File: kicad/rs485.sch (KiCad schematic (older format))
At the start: 7 parts

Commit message: Come back to moldova to finish schematics and begin layout
I've started again from Moldova to discuss with Alexander the details.
I'm now working with schematics requeriments.
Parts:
- U: renamed from U?; value LTC2866 -> LTC2865; footprint (none) -> Package_SO:SSOP-28_5.3x10.2mm_P0.65mm; symbol servo:LTC2866 -> servo:LTC2865
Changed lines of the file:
@@
 $Descr A4 11693 8268
 encoding utf-8
-Sheet 13 16
+Sheet 13 17
 Title "RS485"
 Date "25 10 2019"
@@
 $EndDescr
 $Comp
-L servo:LTC2866 U?
+L servo:LTC2865 U?
 U 1 1 5E1BEB46
 P 3500 2250
 AR Path="/5DE3DF56/5E1BEB46" Ref="U?"  Part="1"
-AR Path="/5E1BAEAA/5E1BEB46" Ref="U?"  Part="1"
-F 0 "U?" H 3500 3050 50  0000 C CNN
-F 1 "LTC2866" H 3500 2950 50  0000 C CNN
-F 2 "" H 4500 1550 50  0001 C CIN
+AR Path="/5E1BAEAA/5E1BEB46" Ref="U"  Part="1"
+F 0 "U" H 3500 3050 50  0000 C CNN
+F 1 "LTC2865" H 3500 2950 50  0000 C CNN
+F 2 "Package_SO:SSOP-28_5.3x10.2mm_P0.65mm" H 4500 1550 50  0001 C CIN
 F 3 "../doc/datasheets/ltc2865.pdf" H 3500 2250 50  0001 C CNN
 	1    3500 2250

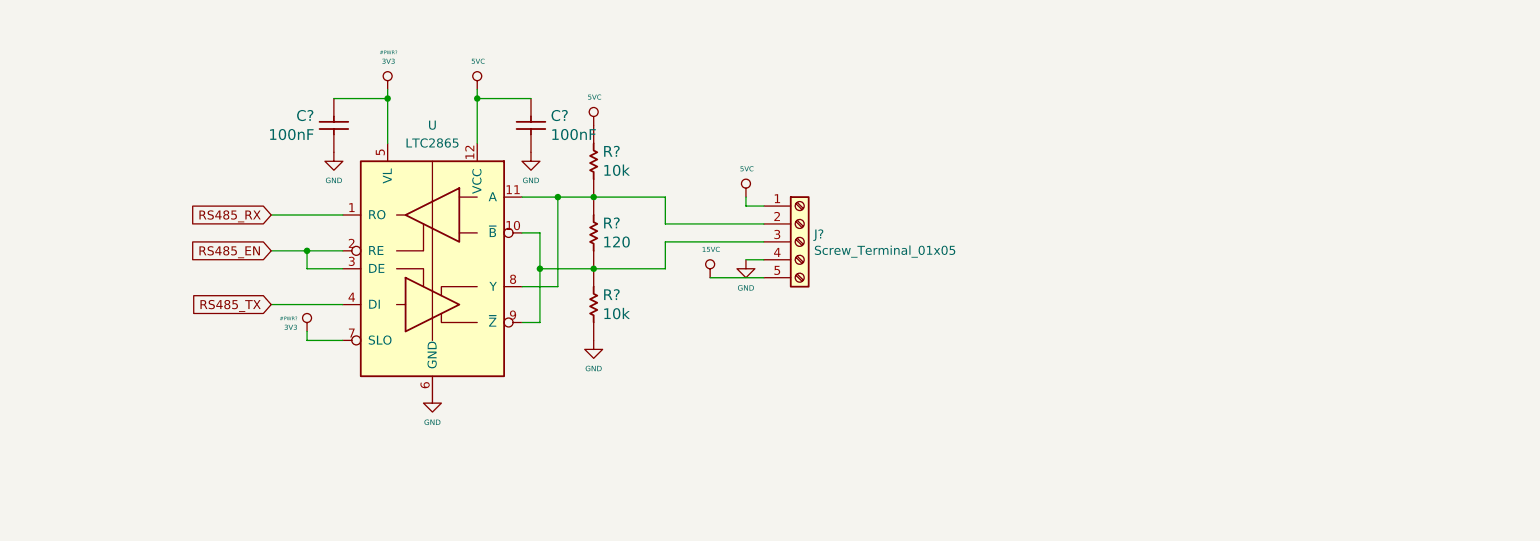
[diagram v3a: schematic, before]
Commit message: changes on ac-in ac/dc -> dc/dc
I've decided to drop out the ac/dc off-line power supply  and include it
on power board. So the MCU board only receive TWO isolated dc voltages in the rango of
8 to 20v and then it generates 5/3v3/1.2 cold and 5v/3v3 hot to the
circuitery.
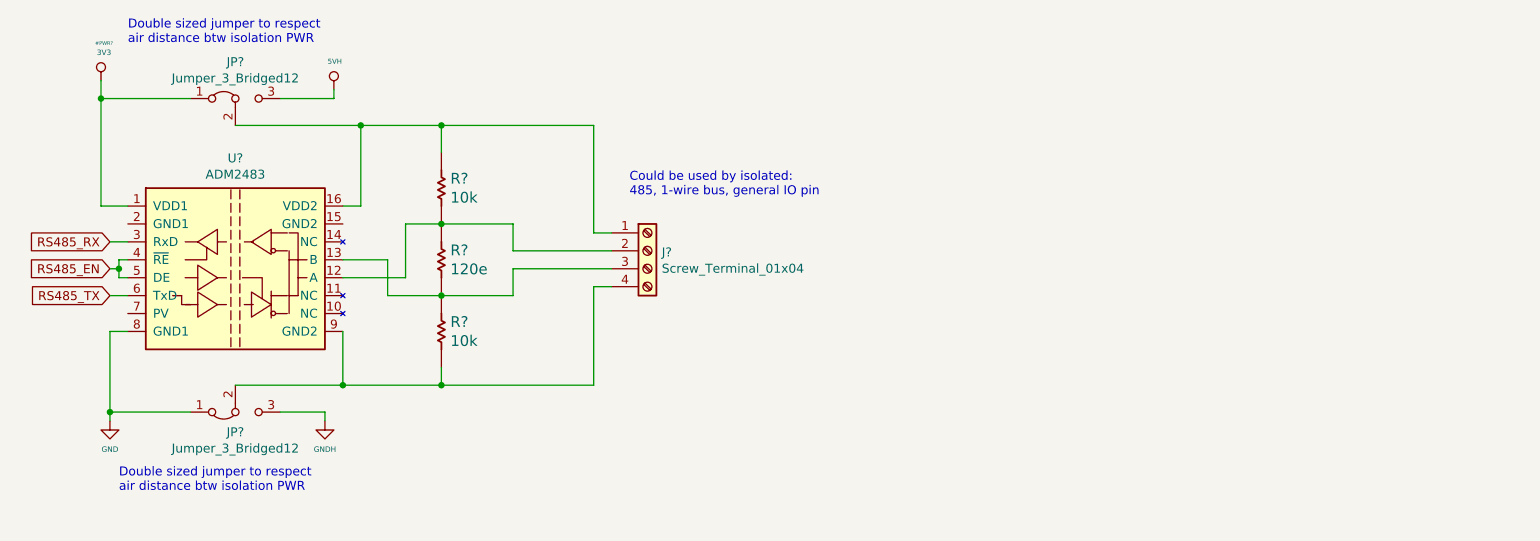
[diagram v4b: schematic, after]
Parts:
- removed C? (x2): 100nF, symbol servo:Capacitor
- removed J?: Screw_Terminal_01x05, symbol Connector:Screw_Terminal_01x05
- removed R?: 120, symbol servo:Resistor
- removed R? (x2): 10k, symbol servo:Resistor
- removed U: LTC2865, Package_SO:SSOP-28_5.3x10.2mm_P0.65mm, symbol servo:LTC2865
- added J?: Screw_Terminal_01x04, symbol Connector:Screw_Terminal_01x04
- added JP? (x2): Jumper_3_Bridged12, symbol Jumper:Jumper_3_Bridged12
- added R?: 120e, symbol servo:Resistor
- added R? (x2): 10k, symbol servo:Resistor
- added U?: ADM2483, Package_SO:SOIC-16W_7.5x10.3mm_P1.27mm, symbol servo:ADM2483
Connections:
- net 3V3: now also JP?.1 (A), U?.1 (VDD1)
- net GND: now also JP?.1 (A), U?.8 (GND1)
- net RS485_EN: now also U?.4 (~RE), U?.5 (DE)
- net RS485_RX: now also U?.3 (RxD)
- net RS485_TX: now also U?.6 (TxD)
- new net: J?.2 (Pin_2), R?.1, R?.2, U?.12 (A)
- new net: J?.3 (Pin_3), R?.1, R?.2, U?.13 (B)
- new net: J?.1 (Pin_1), JP?.2 (C), R?.1, U?.16 (VDD2)
- new net: J?.4 (Pin_4), JP?.2 (C), R?.2, U?.9 (GND2)
- new net 5VH: JP?.3 (B)
- new net GNDH: JP?.3 (B)
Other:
- note added: "Could be used by isolated: \n485, 1-wire bus, general IO pin"
- note added: "Double sized jumper to respect \nair distance btw isolation PWR\n"

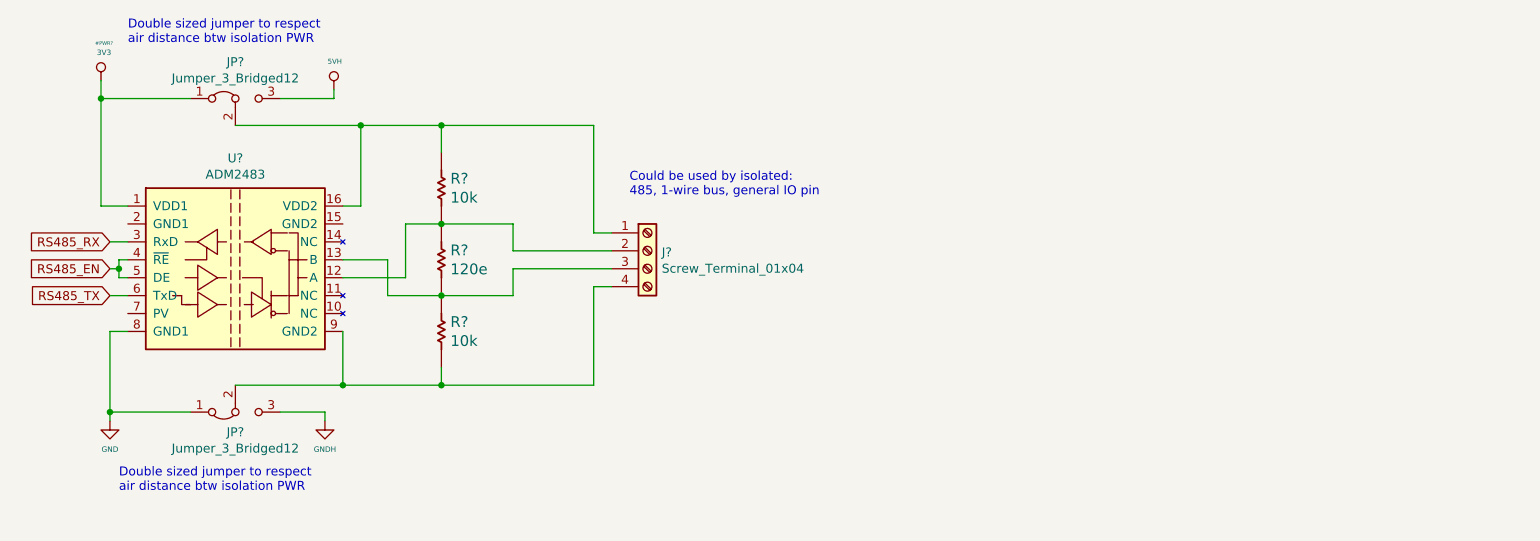
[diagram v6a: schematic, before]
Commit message: I've added LCD UI interfase, EQEP and finish ENDAT
I think I have almos all the interfases ready, I'm begining the
verigication process and then the part definig
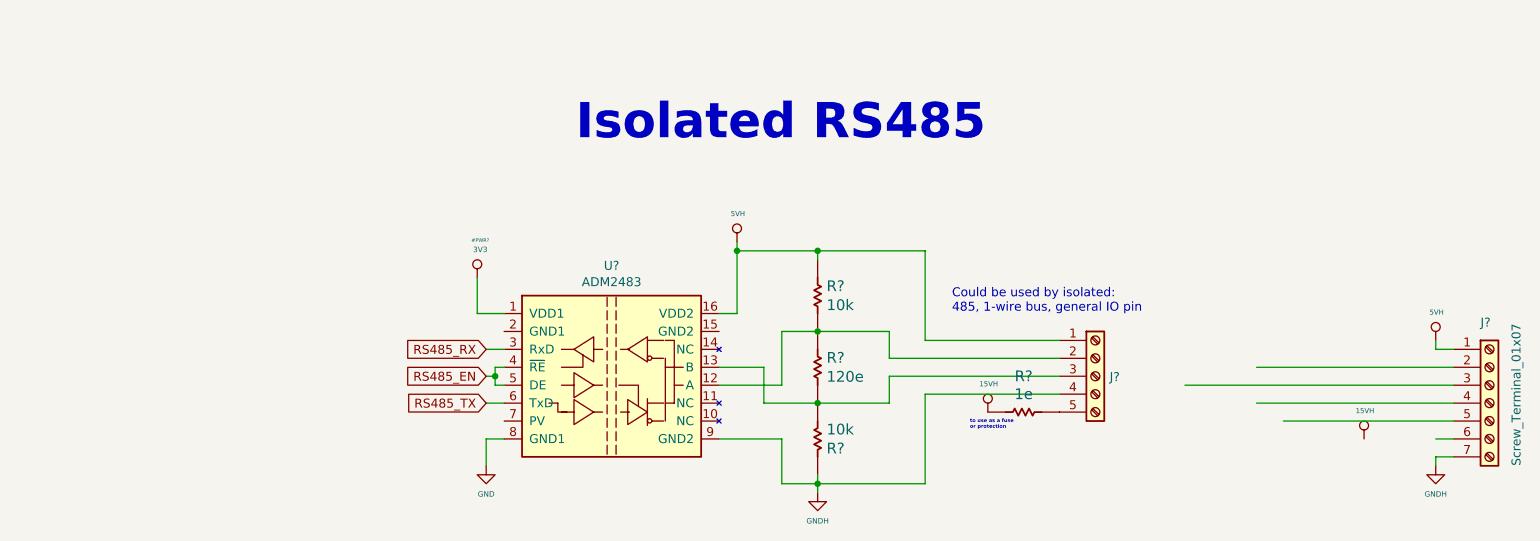
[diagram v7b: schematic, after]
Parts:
- removed J?: Screw_Terminal_01x04, symbol Connector:Screw_Terminal_01x04
- removed JP? (x2): Jumper_3_Bridged12, symbol Jumper:Jumper_3_Bridged12
- added J?: Screw_Terminal_01x07, symbol Connector:Screw_Terminal_01x07
- added J?: Screw_Terminal_01x05, symbol Connector:Screw_Terminal_01x05
- added R?: 1e, symbol servo:Resistor
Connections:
- net labels added: 15VH
- wire segments 46 -> 48
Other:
- note added: "Isolated RS485"
- note added: "to use as a fuse \nor protection"
- note removed: "Double sized jumper to respect \nair distance btw isolation PWR\n"
- moved on the sheet: R?, U?
